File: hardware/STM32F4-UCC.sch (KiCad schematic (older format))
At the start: 34 parts, among them P1 Con P1, P2 Con P2, SW1 BT1, SW2 BT2, SW3 BT3, SW4 BT4, U1 LRTBGFTM

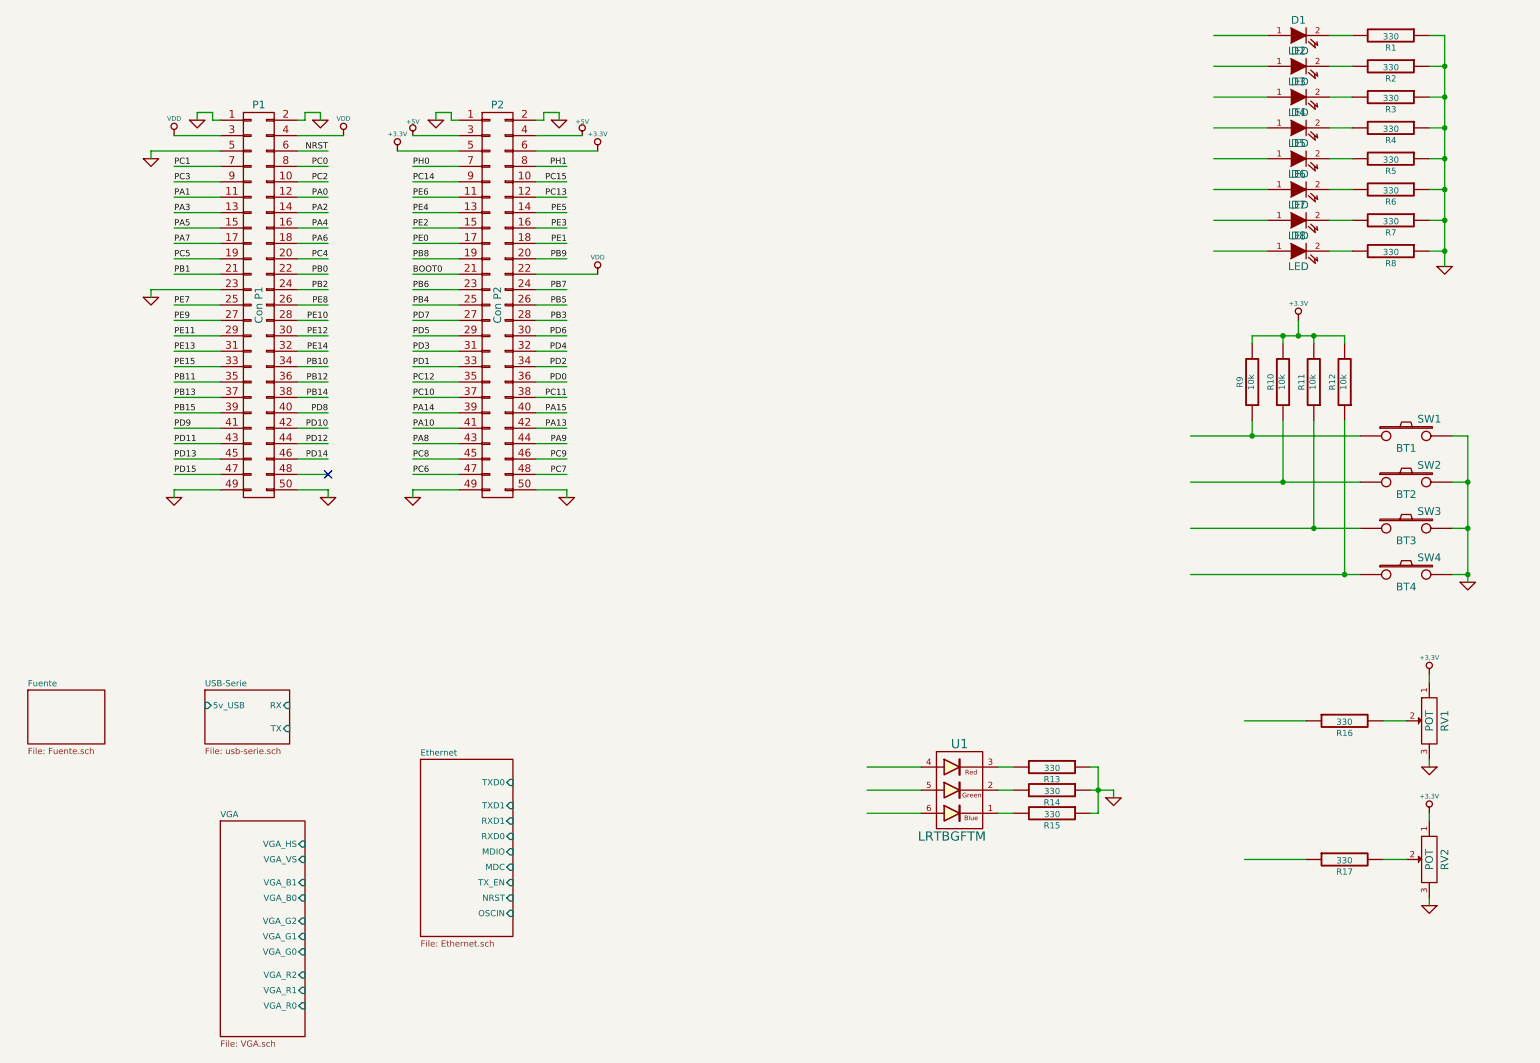
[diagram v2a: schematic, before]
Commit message: Se agrego SD, se colocaron pins en varios modulos, se corrigio orden del VGA
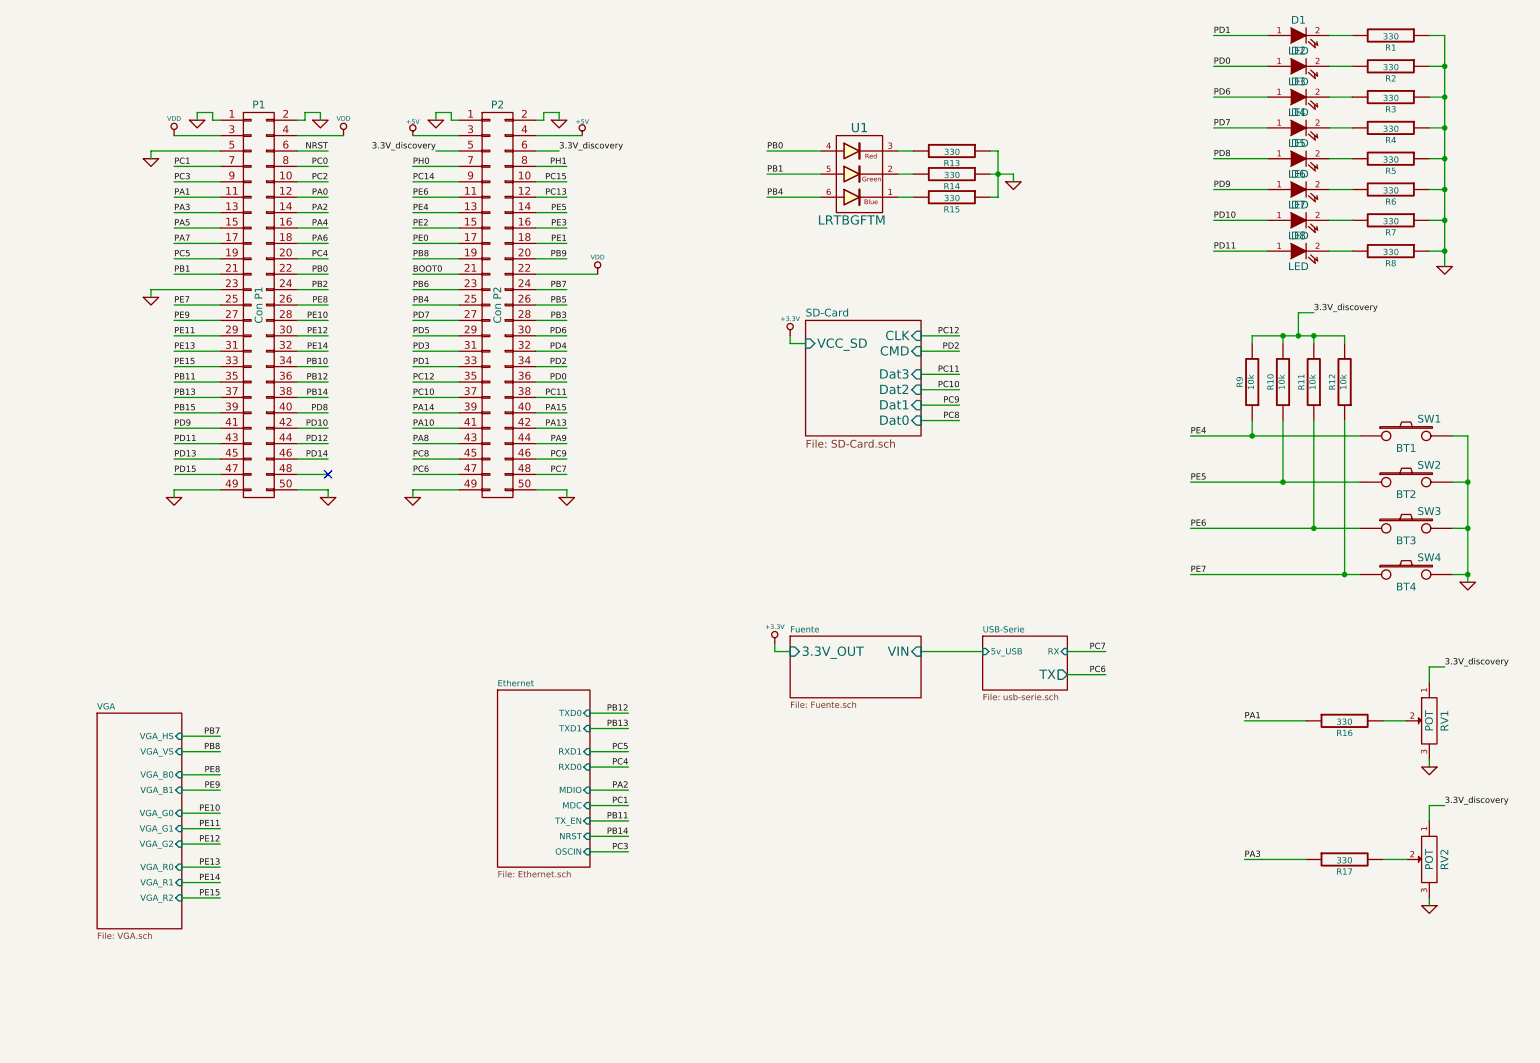
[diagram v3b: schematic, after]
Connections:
- net labels added: 3.3V_discovery
- net labels removed: +3,3V
- wire segments 181 -> 216
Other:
- moved on the sheet: R13, R14, R15, U1

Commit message: Arreglada la distribucion de pines
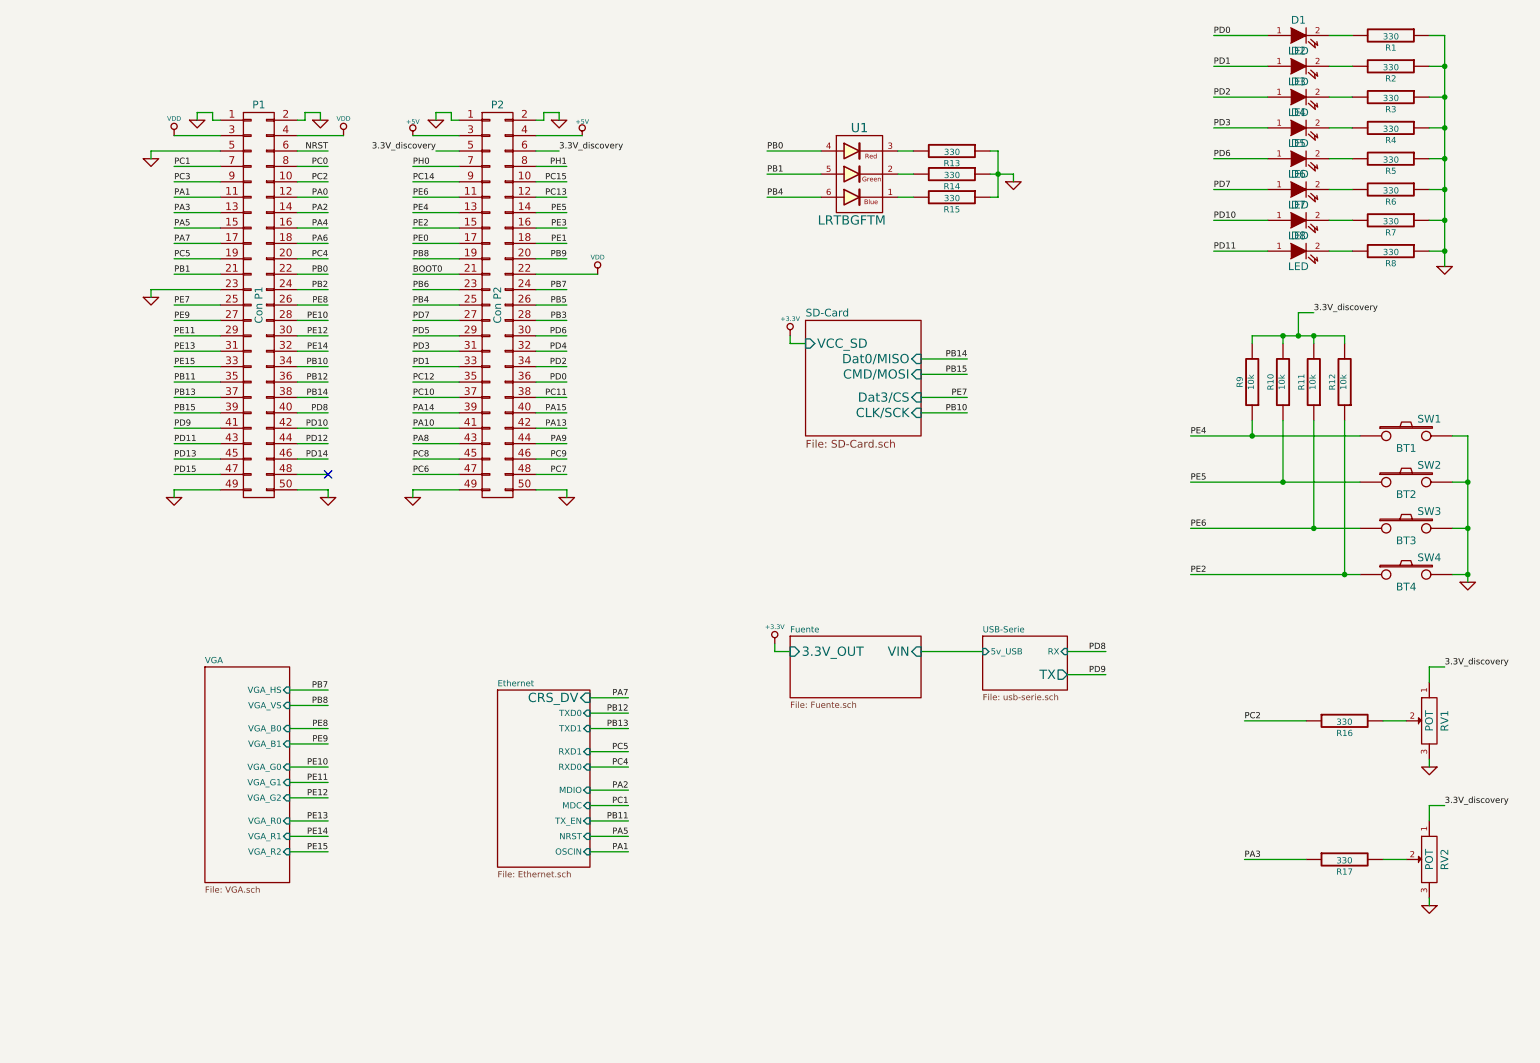
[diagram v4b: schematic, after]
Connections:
- net PA1: no longer R16.1
- net PC2: now also R16.1
- net PD0: now also D1.1 (A); no longer D2.1 (A)
- net PD1: now also D2.1 (A); no longer D1.1 (A)
- net PD2: now also D3.1 (A)
- net PD3: now also D4.1 (A)
- net PD6: now also D5.1 (A); no longer D3.1 (A)
- net PD7: now also D6.1 (A); no longer D4.1 (A)
- net PD8: no longer D5.1 (A)
- net PD9: no longer D6.1 (A)
- net PE2: now also R12.1, SW4.1
- net PE7: no longer R12.1, SW4.1
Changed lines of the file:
@@
 $EndComp
 $Sheet
-S 1600 5200 550  1400
+S 2300 4900 550  1400
 U 538FE9D9
 F0 "VGA" 40
 F1 "VGA.sch" 40
-F2 "VGA_B1" I R 2150 5700 40
-F3 "VGA_B0" I R 2150 5600 40
-F4 "VGA_G2" I R 2150 6050 40
-F5 "VGA_G1" I R 2150 5950 40
-F6 "VGA_G0" I R 2150 5850 40
-F7 "VGA_R2" I R 2150 6400 40
-F8 "VGA_R1" I R 2150 6300 40
-F9 "VGA_R0" I R 2150 6200 40
-F10 "VGA_VS" I R 2150 5450 40
-F11 "VGA_HS" I R 2150 5350 40
+F2 "VGA_B1" I R 2850 5400 40
+F3 "VGA_B0" I R 2850 5300 40
+F4 "VGA_G2" I R 2850 5750 40
+F5 "VGA_G1" I R 2850 5650 40
+F6 "VGA_G0" I R 2850 5550 40
+F7 "VGA_R2" I R 2850 6100 40
+F8 "VGA_R1" I R 2850 6000 40
+F9 "VGA_R0" I R 2850 5900 40
+F10 "VGA_VS" I R 2850 5150 40
+F11 "VGA_HS" I R 2850 5050 40
 $EndSheet
 $Comp
@@
 F9 "NRST" I R 4800 6000 40
 F10 "OSCIN" I R 4800 6100 40
+F11 "CRS_DV" I R 4800 5100 60
 $EndSheet
 $Comp
@@
 Wire Wire Line
 	9400 2600 9500 2600
-Text Label 8150 4950 2    40   ~ 0
-PC6
-Text Label 8150 4800 2    40   ~ 0
-PC7
 Wire Wire Line
 	8150 4950 7900 4950
@@
 PB11
 Text Label 5050 6000 2    40   ~ 0
-PB14
+PA5
 Text Label 5050 6100 2    40   ~ 0
-PC3
-Wire Wire Line
-	2150 5700 2400 5700
-Wire Wire Line
-	2150 5600 2400 5600
-Text Label 2400 5600 2    40   ~ 0
+PA1
+Wire Wire Line
+	2850 5400 3100 5400
+Wire Wire Line
+	2850 5300 3100 5300
+Text Label 3100 5300 2    40   ~ 0
 PE8
-Text Label 2400 5700 2    40   ~ 0
+Text Label 3100 5400 2    40   ~ 0
 PE9
 Wire Wire Line
-	2150 5950 2400 5950
-Wire Wire Line
-	2150 5850 2400 5850
-Text Label 2400 5850 2    40   ~ 0
+	2850 5650 3100 5650
+Wire Wire Line
+	2850 5550 3100 5550
+Text Label 3100 5550 2    40   ~ 0
 PE10
-Text Label 2400 5950 2    40   ~ 0
+Text Label 3100 5650 2    40   ~ 0
 PE11
 Wire Wire Line
-	2150 6300 2400 6300
-Wire Wire Line
-	2150 6200 2400 6200
-Text Label 2400 6200 2    40   ~ 0
+	2850 6000 3100 6000
+Wire Wire Line
+	2850 5900 3100 5900
+Text Label 3100 5900 2    40   ~ 0
 PE13
-Text Label 2400 6300 2    40   ~ 0
+Text Label 3100 6000 2    40   ~ 0
 PE14
 Wire Wire Line
-	2150 6050 2400 6050
-Text Label 2400 6050 2    40   ~ 0
+	2850 5750 3100 5750
+Text Label 3100 5750 2    40   ~ 0
 PE12
 Wire Wire Line
-	2150 6400 2400 6400
-Text Label 2400 6400 2    40   ~ 0
+	2850 6100 3100 6100
+Text Label 3100 6100 2    40   ~ 0
 PE15
 Text Label 5950 1550 0    40   ~ 0
@@
 F0 "SD-Card" 50
 F1 "SD-Card.sch" 50
-F2 "Dat1" I R 6950 3200 60
-F3 "Dat0" I R 6950 3300 60
-F4 "CLK" I R 6950 2750 60
-F5 "CMD" I R 6950 2850 60
-F6 "Dat3" I R 6950 3000 60
-F7 "Dat2" I R 6950 3100 60
-F8 "VCC_SD" I L 6200 2800 60
+F2 "VCC_SD" I L 6200 2800 60
+F3 "Dat0/MISO" I R 6950 2900 60
+F4 "CLK/SCK" I R 6950 3250 60
+F5 "CMD/MOSI" I R 6950 3000 60
+F6 "Dat3/CS" I R 6950 3150 60
 $EndSheet
-Wire Wire Line
-	6950 2850 7200 2850
-Wire Wire Line
-	6950 2750 7200 2750
-Text Label 7200 2750 2    40   ~ 0
-PC12
-Text Label 7200 2850 2    40   ~ 0
-PD2
-Wire Wire Line
-	6950 3100 7200 3100
-Wire Wire Line
-	6950 3000 7200 3000
-Text Label 7200 3000 2    40   ~ 0
-PC11
-Text Label 7200 3100 2    40   ~ 0
-PC10
-Wire Wire Line
-	6950 3300 7200 3300
-Wire Wire Line
-	6950 3200 7200 3200
-Text Label 7200 3200 2    40   ~ 0
-PC9
-Text Label 7200 3300 2    40   ~ 0
-PC8
 $Comp
 L +3.3V #PWR?
@@
 	6100 2800 6100 2750
 Wire Wire Line
-	2150 5450 2400 5450
-Wire Wire Line
-	2150 5350 2400 5350
-Text Label 2400 5350 2    40   ~ 0
+	2850 5150 3100 5150
+Wire Wire Line
+	2850 5050 3100 5050
+Text Label 3100 5050 2    40   ~ 0
 PB7
-Text Label 2400 5450 2    40   ~ 0
+Text Label 3100 5150 2    40   ~ 0
 PB8
 Text Label 9050 5250 0    40   ~ 0
-PA1
+PC2
 Text Label 9050 6150 0    40   ~ 0
 PA3
@@
 Text Label 8700 4000 0    40   ~ 0
 PE6
-Text Label 8700 4300 0    40   ~ 0
+Text Label 7250 3150 2    40   ~ 0
 PE7
+Text Label 8850 1000 0    40   ~ 0
+PD1
 Text Label 8850 800  0    40   ~ 0
-PD1
-Text Label 8850 1000 0    40   ~ 0
 PD0
-Text Label 8850 1200 0    40   ~ 0
+Text Label 8850 1600 0    40   ~ 0
 PD6
-Text Label 8850 1400 0    40   ~ 0
+Text Label 8850 1800 0    40   ~ 0
 PD7
-Text Label 8850 1600 0    40   ~ 0
+Text Label 8150 4800 2    40   ~ 0
 PD8
-Text Label 8850 1800 0    40   ~ 0
+Text Label 8150 4950 2    40   ~ 0
 PD9
 Text Label 8850 2000 0    40   ~ 0
@@
 Text Label 8850 2200 0    40   ~ 0
 PD11
+Text Label 8850 1200 0    40   ~ 0
+PD2
+Text Label 8850 1400 0    40   ~ 0
+PD3
+Wire Wire Line
+	6950 3000 7250 3000
+Wire Wire Line
+	6950 2900 7250 2900
+Wire Wire Line
+	6950 3250 7250 3250
+Wire Wire Line
+	6950 3150 7250 3150
+Text Label 7250 3250 2    40   ~ 0
+PB10
+Text Label 8700 4300 0    40   ~ 0
+PE2
+Text Label 7250 3000 2    40   ~ 0
+PB15
+Text Label 7250 2900 2    40   ~ 0
+PB14
+Wire Wire Line
+	4800 5100 5050 5100
+Text Label 5050 5100 2    40   ~ 0
+PA7
 $EndSCHEMATC

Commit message: Terminado el esquematico, iniciado el PCB
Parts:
- added D11: POWER, LEDs:LED-0805, symbol LED
- added R48: 330, Resistors_SMD:Resistor_SMD1206_ReflowWave, symbol R
- D1, D2, D3, D4, D5, D6, D7, D8: footprint (none) -> LEDs:LED-0805
- P1, P2: footprint (none) -> Pin_Headers:Pin_Header_Straight_2x25
- R1, R10, R11, R12, R13, R14, R15, R16, R17, R2, R3, R4, R5, R6, R7, R8, R9: footprint (none) -> Resistors_SMD:Resistor_SMD1206_ReflowWave
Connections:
- net +3.3V: now also R48.2
- net GND: now also D11.2 (K)
- new net: D11.1 (A), R48.1

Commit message: Terminado el Routeo de la Placa
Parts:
- removed P1: Con P1, Pin_Headers:Pin_Header_Straight_2x25, symbol CONN_02X25
- removed P2: Con P2, Pin_Headers:Pin_Header_Straight_2x25, symbol CONN_02X25
- removed R17: 330, Resistors_SMD:Resistor_SMD1206_ReflowWave, symbol R
- removed RV2: POT, symbol POT
- removed U1: LRTBGFTM, symbol ASMT-YTC2-0AA02
- added J2: STM32F4_Discovery_Header, w_Connectors:stm32f4_discovery_header, symbol STM32F4_Discovery_Header
- added JP1: Alimentacion, Pin_Headers:Pin_Header_Straight_1x03, symbol JUMPER3
- added R2, R3: 0, Resistors_SMD:R_0805, symbol R
- added U1: PLCC4, w_Connectors:PLCC4, symbol PLCC4
- D2: renamed from D1; value LED -> L1
- D3: renamed from D2; value LED -> L2
- R1: renamed from R48; footprint Resistors_SMD:Resistor_SMD1206_ReflowWave -> Resistors_SMD:R_0805
- R10: renamed from R12; footprint Resistors_SMD:Resistor_SMD1206_ReflowWave -> Resistors_SMD:R_0805
- R11: renamed from R16; footprint Resistors_SMD:Resistor_SMD1206_ReflowWave -> Resistors_SMD:R_0805
- R12: renamed from R1; footprint Resistors_SMD:Resistor_SMD1206_ReflowWave -> Resistors_SMD:R_0805
- R13: renamed from R2; footprint Resistors_SMD:Resistor_SMD1206_ReflowWave -> Resistors_SMD:R_0805
- R14: renamed from R3; footprint Resistors_SMD:Resistor_SMD1206_ReflowWave -> Resistors_SMD:R_0805
- R15: renamed from R4; footprint Resistors_SMD:Resistor_SMD1206_ReflowWave -> Resistors_SMD:R_0805
- R16: renamed from R5; footprint Resistors_SMD:Resistor_SMD1206_ReflowWave -> Resistors_SMD:R_0805
- R17: renamed from R6; footprint Resistors_SMD:Resistor_SMD1206_ReflowWave -> Resistors_SMD:R_0805
- R18: renamed from R7; footprint Resistors_SMD:Resistor_SMD1206_ReflowWave -> Resistors_SMD:R_0805
- R19: renamed from R8; footprint Resistors_SMD:Resistor_SMD1206_ReflowWave -> Resistors_SMD:R_0805
- R4: renamed from R13; footprint Resistors_SMD:Resistor_SMD1206_ReflowWave -> Resistors_SMD:R_0805
- R5: renamed from R14; footprint Resistors_SMD:Resistor_SMD1206_ReflowWave -> Resistors_SMD:R_0805
- R6: renamed from R15; footprint Resistors_SMD:Resistor_SMD1206_ReflowWave -> Resistors_SMD:R_0805
- R7: renamed from R9; footprint Resistors_SMD:Resistor_SMD1206_ReflowWave -> Resistors_SMD:R_0805
- R8: renamed from R10; footprint Resistors_SMD:Resistor_SMD1206_ReflowWave -> Resistors_SMD:R_0805
- R9: renamed from R11; footprint Resistors_SMD:Resistor_SMD1206_ReflowWave -> Resistors_SMD:R_0805
- RV1: footprint (none) -> w_Connectors:POTE
- SW1, SW2, SW3, SW4: footprint (none) -> w_switch:PCB_PUSH; symbol SW_PUSH -> SW_PUSH_2
- renumbered D11 to D1, D3 to D4, D4 to D5, D5 to D6, D6 to D7, D7 to D8, D8 to D9
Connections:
- net +3.3V: now also R10.2, R7.2, R8.2, R9.2, JP1.2, R2.1, R3.1, U1.2 (AR)
- net +5V: now also J2.97 (5V), J2.98 (5V)
- net 3.3V_discovery: now also J2.95 (3V), J2.96 (3V), JP1.3, R2.2; no longer R10.2, R7.2, R8.2, R9.2
- net GND: now also SW1.4, SW2.4, SW3.4, SW4.4, J2.1 (GND), J2.100 (GND), J2.2 (GND), J2.23 (GND), J2.49 (GND), J2.5 (GND), J2.50 (GND), J2.51 (GND), J2.52 (GND), J2.99 (GND); no longer R4.1, R5.1, R6.1
- net PA0: now also J2.12 (PA0)
- net PA1: now also J2.11 (PA1)
- net PA10: now also J2.59 (PA10)
- net PA13: now also J2.60 (PA13)
- net PA14: now also J2.61 (PA14)
- net PA15: now also J2.62 (PA15)
- net PA2: now also J2.14 (PA2)
- net PA3: now also J2.13 (PA3)
- net PA4: now also J2.16 (PA4)
- net PA5: now also J2.15 (PA5)
- net PA6: now also J2.18 (PA6)
- net PA7: now also J2.17 (PA7)
- net PA8: now also J2.57 (PA8)
- net PA9: now also J2.58 (PA9)
- net PB0: now also R4.2, J2.22 (PB0)
- net PB1: now also R5.1, J2.21 (PB1)
- net PB10: now also J2.34 (PB10)
- net PB11: now also J2.35 (PB11)
- net PB12: now also J2.36 (PB12)
- net PB13: now also J2.37 (PB13)
- net PB14: now also J2.38 (PB14)
- net PB15: now also J2.39 (PB15)
- net PB2: now also J2.24 (PB2)
- net PB3: now also J2.74 (PB3)
- net PB4: now also R6.1, J2.75 (PB4)
- net PB5: now also J2.76 (PB5)
- net PB6: now also J2.77 (PB6)
- net PB7: now also J2.78 (PB7)
- net PB8: now also J2.81 (PB8)
- net PB9: now also J2.82 (PB9)
- net PC0: now also J2.8 (PC0)
- net PC1: now also J2.7 (PC1)
- net PC10: now also J2.63 (PC10)
- net PC11: now also J2.64 (PC11)
- net PC12: now also J2.65 (PC12)
- net PC13: now also J2.90 (PC13)
- net PC14: now also J2.91 (PC14)
- net PC15: now also J2.92 (PC15)
- net PC2: now also J2.10 (PC2)
- net PC3: now also J2.9 (PC3)
- net PC4: now also J2.20 (PC4)
- net PC5: now also J2.19 (PC5)
- net PC6: now also J2.53 (PC6)
- net PC7: now also J2.54 (PC7)
- net PC8: now also J2.55 (PC8)
- net PC9: now also J2.56 (PC9)
- net PD0: now also J2.66 (PD0)
- net PD1: now also J2.67 (PD1)
- net PD10: now also J2.42 (PD10)
- net PD11: now also J2.43 (PD11)
- net PD12: now also J2.44 (PD12)
- net PD13: now also J2.45 (PD13)
- net PD14: now also J2.46 (PD14)
- net PD15: now also J2.47 (PD15)
- net PD2: now also J2.68 (PD2)
- net PD3: now also J2.69 (PD3)
- net PD4: now also J2.70 (PD4)
- net PD5: now also J2.71 (PD5)
- net PD6: now also J2.72 (PD6)
- net PD7: now also J2.73 (PD7)
- net PD8: now also J2.40 (PD8)
- net PD9: now also J2.41 (PD9)
- net PE0: now also J2.83 (PE0)
- net PE1: now also J2.84 (PE1)
- net PE10: now also J2.28 (PE10)
- net PE11: now also J2.29 (PE11)
- net PE12: now also J2.30 (PE12)
- net PE13: now also J2.31 (PE13)
- net PE14: now also J2.32 (PE14)
- net PE15: now also J2.33 (PE15)
- net PE2: now also SW4.3, J2.85 (PE2)
- net PE3: now also J2.86 (PE3)
- net PE4: now also SW1.3, J2.87 (PE4)
- net PE5: now also SW2.3, J2.88 (PE5)
- net PE6: now also SW3.3, J2.89 (PE6)
- net PE7: now also J2.25 (PE7)
- net PE8: now also J2.26 (PE8)
- net PE9: now also J2.27 (PE9)
- net PH0: now also J2.93 (PH0)
- net PH1: now also J2.94 (PH1)
- net at R6.2: now also U1.3 (KB)
- net at R5.2: now also U1.4 (KG)
- new net: R4.1, U1.1 (AR)
- new net Fuente/3.3V_OUT: JP1.1, R3.2
- no-connect marks 1 -> 6
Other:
- moved on the sheet: R10, R11, R4, R5, R6, R7, R8, R9, RV1
